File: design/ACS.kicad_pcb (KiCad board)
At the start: 4 copper layers, 60 x 45 mm, 87 parts, among them IC1 ADXL375BCCZ, IC2 I3G4250DTR, IC3 TPS56A37RPAR, IC4 74HCT126D,653, J1 SM06B-SRSS-TBLFSN, J2 XT30, J3 USB_C_Receptacle_USB2.0_14P, J4 SM04B-SRSS-TB, M1 Servo_W, M2 Servo_S, M3 Servo_E, M4 Servo_N, U1 STM32U575CGUx, U2 USBLC6-2SC6, U3 SN65HVD232, Y1 16MHz

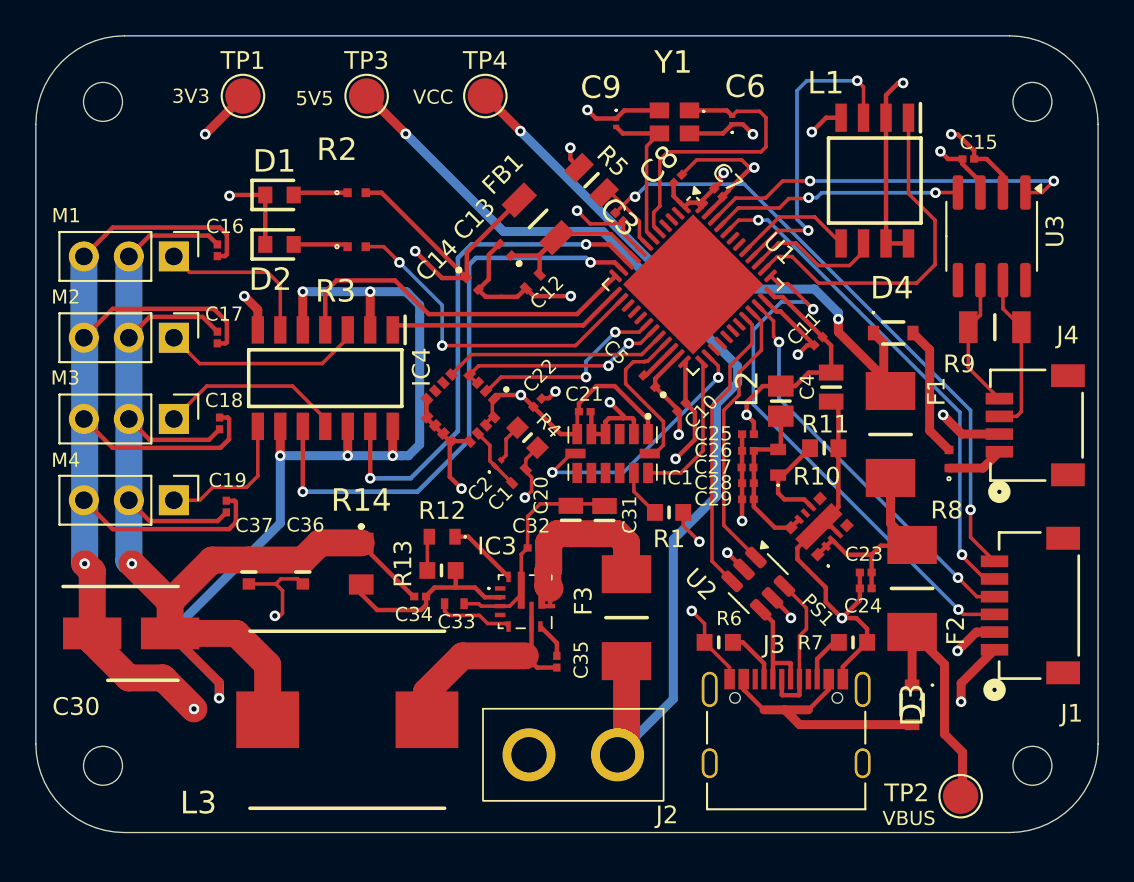
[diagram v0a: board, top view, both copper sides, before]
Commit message: fix footprint assignment and add BOM
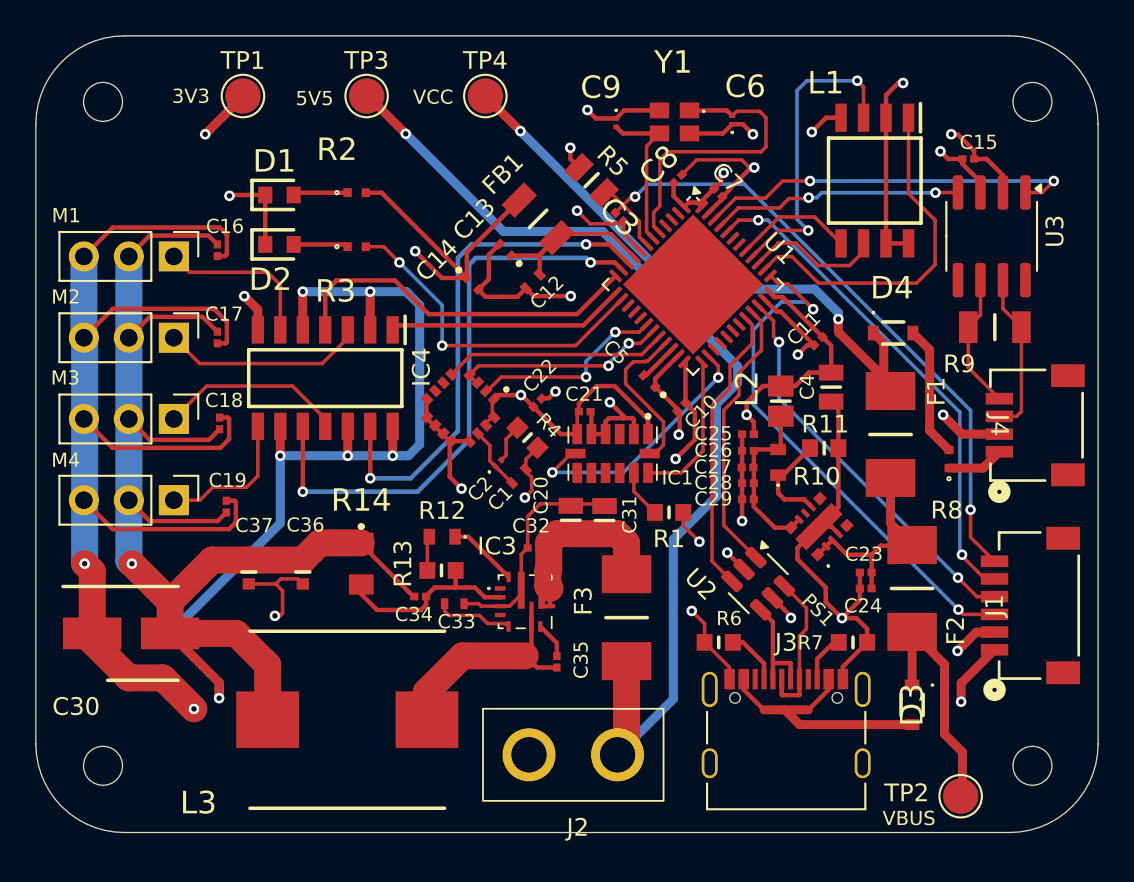
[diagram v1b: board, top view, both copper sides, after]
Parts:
- J1: footprint ACS:CONN_SM06B-SRSS-TB_JST -> footprints:CONN_SM06B-SRSS-TB_JST
- J2: footprint ACS:XT30 -> footprints:XT30
- J3: footprint Connector_USB:USB_C_Receptacle_Palconn_UTC16-G -> footprints:USB_C_Receptacle_Palconn_UTC16-G fixed
- J4: footprint ACS:CONN_SM04B-SRSS-TB_JST -> footprints:CONN_SM04B-SRSS-TB_JST
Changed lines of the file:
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@@
 		)
 	)
-	(footprint "ACS:XT30"
+	(footprint "footprints:XT30"
 		(layer "F.Cu")
 		(at 136.565 119.38)
 		(property "Reference" "J2"
-			(at 5.294 3.4036 0)
+			(at 0.254 4.112 0)
 			(unlocked yes)
 			(layer "F.SilkS")
@@
 		)
 		(property "Value" "XT30"
-			(at -3.342 3.6322 0)
+			(at 0.254 5.612 0)
 			(unlocked yes)
 			(layer "F.Fab")
@@
 		)
 		(fp_text user "${REFERENCE}"
-			(at 5.548 3.5814 0)
+			(at 0.254 7.112 0)
 			(unlocked yes)
 			(layer "F.Fab")
@@
 		(embedded_fonts no)
 	)
-	(footprint "ACS:CONN_SM04B-SRSS-TB_JST"
+	(footprint "footprints:CONN_SM04B-SRSS-TB_JST"
 		(layer "F.Cu")
 		(at 162.7281 100.7632 -90)
 		(tags "SM04B-SRSS-TB ")
 		(property "Reference" "J4"
-			(at -5.0814 -1.7623 0)
+			(at 0 2.0985 270)
 			(unlocked yes)
 			(layer "F.SilkS")
@@
 		)
 		(property "Datasheet" "SM04B-SRSS-TB"
-			(at 0 0 90)
+			(at 0 0 270)
 			(layer "F.Fab")
 			(hide yes)
@@
 		)
 		(property "Description" ""
-			(at 0 0 90)
+			(at 0 0 270)
 			(layer "F.Fab")
 			(hide yes)
@@
 		)
 	)
-	(footprint "Connector_USB:USB_C_Receptacle_Palconn_UTC16-G"
+	(footprint "footprints:USB_C_Receptacle_Palconn_UTC16-G fixed"
 		(layer "F.Cu")
 		(at 148.59 117.616)
@@
 		(tags "USB C Type-C Receptacle USB2.0")
 		(property "Reference" "J3"
-			(at -0.6858 -4.459 0)
+			(at 0 -4.58 0)
 			(layer "F.SilkS")
 			(effects
@@
 		)
 		(property "Value" "USB_C_Receptacle_USB2.0_14P"
-			(at -0.127 3.669 0)
+			(at 0 6.24 0)
 			(layer "F.Fab")
 			(effects
@@
 		(sheetname "/")
 		(sheetfile "ACS.kicad_sch")
+		(clearance 0.1)
 		(attr smd)
 		(fp_line
@@
 		)
 		(fp_text user "${REFERENCE}"
-			(at 5.8928 5.3454 0)
+			(at 0 1.18 0)
 			(layer "F.Fab")
 			(effects
@@
 			(drill 0.6)
 			(layers "F&B.Cu" "*.Mask")
+			(clearance 0)
 		)
 		(pad "" np_thru_hole circle
@@
 			(size 0.6 0.6)
 			(drill 0.6)
-			(layers "*.Cu" "*.Mask")
+			(layers "F&B.Cu" "*.Mask")
+			(clearance 0)
 		)
 		(pad "A1" smd rect
@@
 			(layers "*.Cu" "*.Mask")
 			(remove_unused_layers no)
-			(net 35 "unconnected-(J3-SHIELD-PadS1)_1")
+			(net 32 "unconnected-(J3-SHIELD-PadS1)")
 			(pinfunction "SHIELD")
 			(pintype "passive+no_connect")
@@
 			(layers "*.Cu" "*.Mask")
 			(remove_unused_layers no)
-			(net 32 "unconnected-(J3-SHIELD-PadS1)")
+			(net 35 "unconnected-(J3-SHIELD-PadS1)_1")
 			(pinfunction "SHIELD")
 			(pintype "passive+no_connect")
@@
 		)
 	)
-	(footprint "ACS:CONN_SM06B-SRSS-TB_JST"
+	(footprint "footprints:CONN_SM06B-SRSS-TB_JST"
 		(layer "F.Cu")
 		(at 162.8648 110.9472 90)
 		(tags "SM06B-SRSS-TBLFSN ")
 		(property "Reference" "J1"
-			(at -6.096 1.8542 0)
+			(at 0 -2.506701 90)
 			(unlocked yes)
 			(layer "F.SilkS")

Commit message: add gnd test
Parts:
- added TP5: TestPoint, TestPoint:TestPoint_Pad_D2.0mm, F.Cu at (112.9, 86.8)
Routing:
- net Earth: track 209.7 -> 213.4 mm, vias 25 -> 26
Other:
- board text added: "GND"
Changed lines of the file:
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@@
 		)
 	)
+	(footprint "TestPoint:TestPoint_Pad_D2.0mm"
+		(layer "F.Cu")
+		(at 112.8522 86.832)
+		(descr "SMD pad as test Point, diameter 2.0mm")
+		(tags "test point SMD pad")
+		(property "Reference" "TP5"
+			(at 0 -1.998 0)
+			(layer "F.SilkS")
+			(effects
+				(font
+					(size 1 1)
+					(thickness 0.15)
+				)
+			)
+		)
+		(property "Value" "TestPoint"
+			(at 0 2.05 0)
+			(layer "F.Fab")
+			(effects
+				(font
+					(size 1 1)
+					(thickness 0.15)
+				)
+			)
+		)
+		(property "Datasheet" "~"
+			(at 0 0 0)
+			(unlocked yes)
+			(layer "F.Fab")
+			(hide yes)
+			(effects
+				(font
+					(size 1.27 1.27)
+					(thickness 0.15)
+				)
+			)
+		)
+		(property "Description" "test point"
+			(at 0 0 0)
+			(unlocked yes)
+			(layer "F.Fab")
+			(hide yes)
+			(effects
+				(font
+					(size 1.27 1.27)
+					(thickness 0.15)
+				)
+			)
+		)
+		(property ki_fp_filters "Pin* Test*")
+		(sheetname "/")
+		(sheetfile "ACS.kicad_sch")
+		(attr exclude_from_pos_files)
+		(fp_circle
+			(center 0 0)
+			(end 0 1.2)
+			(stroke
+				(width 0.12)
+				(type solid)
+			)
+			(fill no)
+			(layer "F.SilkS")
+		)
+		(fp_circle
+			(center 0 0)
+			(end 1.5 0)
+			(stroke
+				(width 0.05)
+				(type solid)
+			)
+			(fill no)
+			(layer "F.CrtYd")
+		)
+		(fp_text user "${REFERENCE}"
+			(at 0 -2 0)
+			(layer "F.Fab")
+			(effects
+				(font
+					(size 1 1)
+					(thickness 0.15)
+				)
+			)
+		)
+		(pad "1" smd circle
+			(at 0 0)
+			(size 2 2)
+			(layers "F.Cu" "F.Mask")
+			(net 1 "Earth")
+			(pinfunction "1")
+			(pintype "passive")
+		)
+		(embedded_fonts no)
+	)
 	(footprint "SamacSys_Parts:GRM033D70J224ME01D"
 		(layer "F.Cu")
@@
 			(layers "*.Cu" "*.Mask")
 			(remove_unused_layers no)
-			(net 32 "unconnected-(J3-SHIELD-PadS1)")
+			(net 37 "unconnected-(J3-SHIELD-PadS1)_2")
 			(pinfunction "SHIELD")
 			(pintype "passive+no_connect")
@@
 			(layers "*.Cu" "*.Mask")
 			(remove_unused_layers no)
-			(net 37 "unconnected-(J3-SHIELD-PadS1)_2")
+			(net 32 "unconnected-(J3-SHIELD-PadS1)")
 			(pinfunction "SHIELD")
 			(pintype "passive+no_connect")
@@
 		)
 	)
+	(gr_text "GND"
+		(at 114.6556 86.8426 0)
+		(layer "F.SilkS")
+		(effects
+			(font
+				(size 0.8 0.8)
+				(thickness 0.1)
+			)
+			(justify left bottom)
+		)
+	)
 	(gr_text "5V5"
 		(at 120.8786 82.7786 0)
@@
 	)
 	(segment
+		(start 112.8522 86.832)
+		(end 109.2052 86.832)
+		(width 0.254)
+		(layer "F.Cu")
+		(net 1)
+	)
+	(segment
 		(start 133.8834 103.251)
 		(end 133.8834 102.6926)
@@
 	)
 	(segment
+		(start 109.2052 86.832)
+		(end 109.1946 86.8426)
+		(width 0.254)
+		(layer "F.Cu")
+		(net 1)
+	)
+	(segment
 		(start 110.553 89.597)
 		(end 108.92 91.23)
@@
 		(size 0.6)
 		(drill 0.3)
+		(layers "F.Cu" "B.Cu")
+		(net 1)
+	)
+	(via
+		(at 109.1946 86.8426)
+		(size 0.6)
+		(drill 0.3)

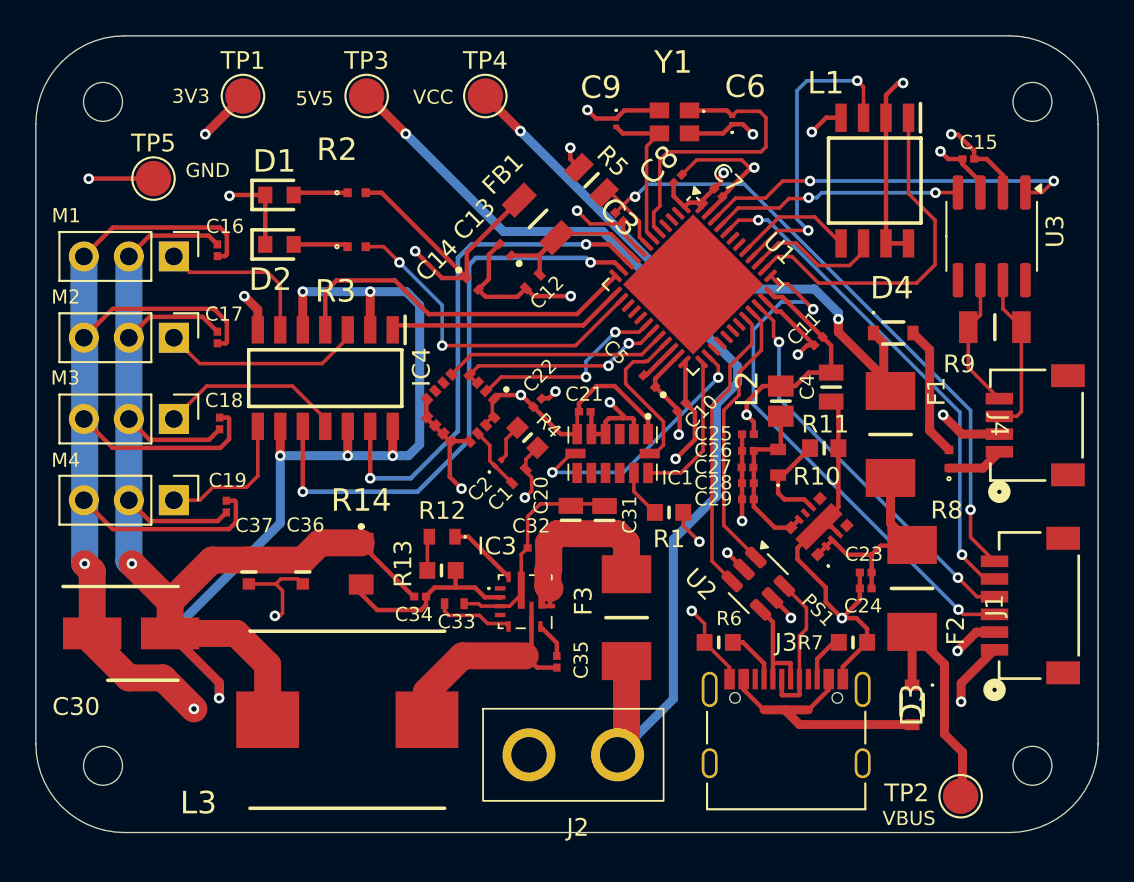
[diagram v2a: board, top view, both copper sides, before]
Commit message: move servo 5V5 and GND to F
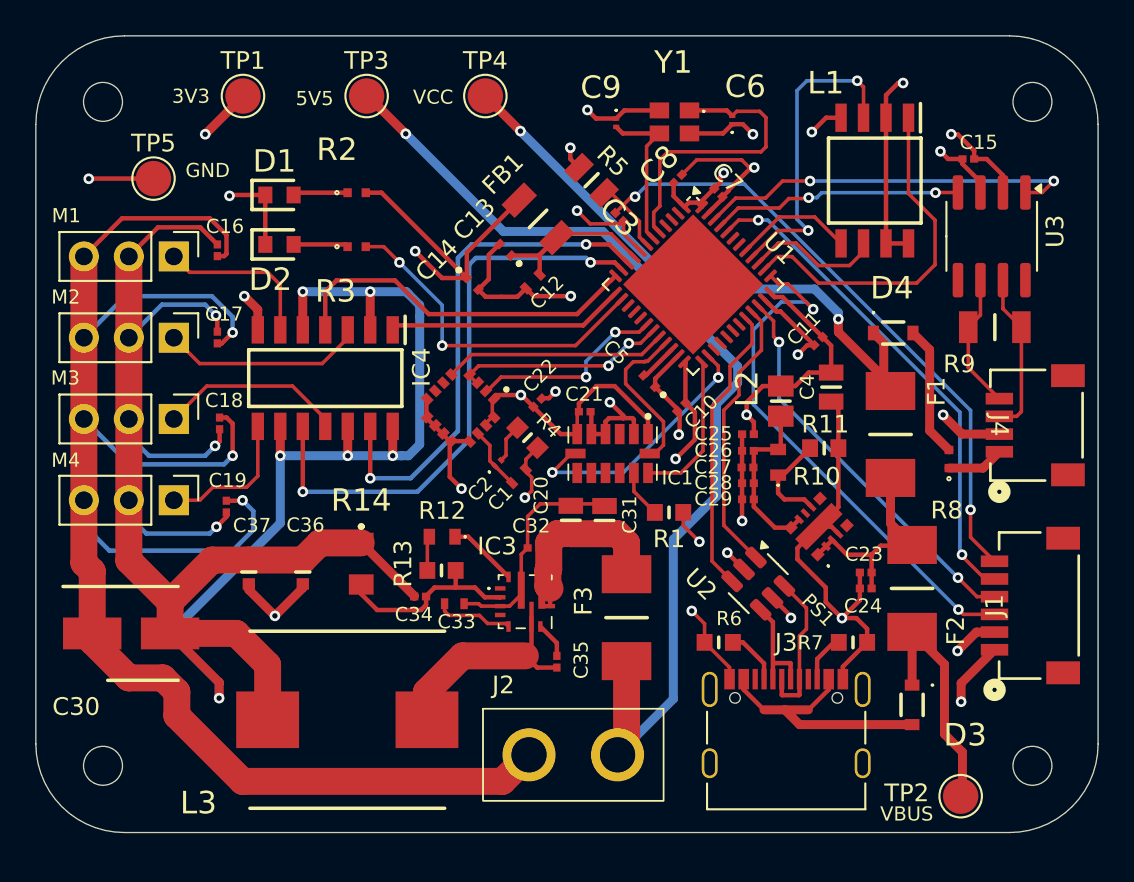
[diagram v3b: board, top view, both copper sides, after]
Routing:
- net Earth: track 213.4 -> 241.5 mm, vias 26 -> 27
- net +5V5: track 125.7 -> 130.2 mm, vias 7 -> 9

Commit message: design review fixes
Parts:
- moved C12 4.86 mm to (138.1, 89.6), turned to 135 degrees
- moved FB1 2.88 mm to (133.5, 91.8)
- moved C13 2.66 mm to (135.0, 89.6)
- moved C15 1.30 mm to (160.2, 85.9)
- moved C14 0.92 mm to (130.1, 92.2), turned to 135 degrees
- moved C10 0.26 mm to (142.8, 99.5)
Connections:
- J3 pad S1: unconnected-(J3-SHIELD-PadS1)_3 -> Earth
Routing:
- net Earth: track 241.5 -> 146.7 mm, vias 27 -> 28
- net +3V3: track 81.3 -> 68.2 mm, vias 11 -> 10
- net /SERVO_PWM_N: track 29.1 -> 26.0 mm
- net /SERVO_PWM_E: track 33.3 -> 30.2 mm
- net +3V3A: track 10.9 -> 8.52 mm
- net +5V5: track 130.2 -> 128.4 mm, vias 9 -> 6
- net /SWCLK: track 30.1 -> 28.8 mm
- net /NRST: track 39.4 -> 40.7 mm
- net /ACC_SDIO: track 8.68 -> 9.39 mm
- net Net-(IC4-3Y): track 8.12 -> 7.51 mm
- net /CAN_TX: track 21.9 -> 22.5 mm

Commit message: design review fixes
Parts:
- removed the C25 at (146.4, 101.3)
- removed the C26 at (146.4, 102.2)
- removed the C27 at (146.4, 103.1)
- removed the L2 at (148.3, 99.4)
- added C11: 22u, SamacSys_Parts:GRM18x, F.Cu at (147.6, 104.4)
- added C35: 100n, SamacSys_Parts:CAPC0603X35N, F.Cu at (126.7, 102.5)
- added C36: 100n, SamacSys_Parts:CAPC0603X35N, F.Cu at (121.0, 93.6)
- added C37: 100n, SamacSys_Parts:CAPC0603X35N, F.Cu at (124.7, 93.6)
- C28, C29: value 4u7 -> 100n; footprint SamacSys_Parts:CAPC0603X55N -> SamacSys_Parts:CAPC0603X35N
- moved C29 26.9 mm to (119.7, 102.5), turned to 180 degrees
- moved C28 23.0 mm to (123.5, 102.4), turned to 180 degrees
- moved R3 3.04 mm to (150.7, 101.2), turned to 180 degrees
- moved C17 2.60 mm to (142.9, 83.4), turned to -45 degrees
- moved U2 2.46 mm to (148.3, 111.8), turned to -90 degrees
- moved Y1 2.33 mm to (140.7, 85.4), turned to 135 degrees
- moved R11 1.75 mm to (143.0, 113.1)
- moved C5 1.67 mm to (153.2, 110.7)
- moved C4 1.60 mm to (153.2, 111.6)
- moved F2 1.35 mm to (154.4, 99.9)
- moved D4 1.33 mm to (154.8, 94.2)
- moved F3 1.13 mm to (155.8, 108.9)
- moved PS1 1.11 mm to (151.5, 106.5), turned to 180 degrees
- moved C16 0.99 mm to (151.2, 97.6)
- moved C20 0.99 mm to (143.5, 86.8)
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- renumbered C21 to C1, C22 to C10, C36 to C12, C1 to C13, C2 to C14, C37 to C15, C4 to C16, C6 to C17, C7 to C18, C3 to C19, C20 to C2, C8 to C20, C9 to C21, C5 to C22, C10 to C23, C11 to C24, C12 to C25, C13 to C26, C14 to C27, C31 to C3, C16 to C30, C17 to C31, C18 to C32, C15 to C33, C19 to C34, C30 to C38, C24 to C4, C23 to C5, C32 to C6, C33 to C7, C35 to C8, C34 to C9, F3 to F1, F1 to F2, F2 to F3, IC3 to IC2, IC2 to IC3, J2 to J1, J1 to J2, L3 to L2, R12 to R1, R5 to R10, R6 to R11, R7 to R12, R8 to R13, R9 to R14, R1 to R2, R10 to R3, R11 to R4, R14 to R5, R13 to R6, R2 to R7, R3 to R8, R4 to R9, TP3 to TP1, TP4 to TP2, TP2 to TP3, TP5 to TP4, TP1 to TP5
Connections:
- C1 pad 1: +3V3 -> +3V3A
- C10 pad 1: +3V3 -> +3V3A
- C28 pad 1: Earth -> +5V5
- C28 pad 2: Net-(PS1-VOUT_1) -> Earth
- C29 pad 1: Earth -> +5V5
- C29 pad 2: Net-(PS1-VOUT_1) -> Earth
- IC1 pad 1: +3V3 -> +3V3A
- IC1 pad 6: +3V3 -> +3V3A
- IC3 pad 1: +3V3 -> +3V3A
- IC3 pad 15: +3V3 -> +3V3A
- IC3 pad 16: +3V3 -> +3V3A
- PS1 pad 10: Net-(PS1-VOUT_1) -> +3V3
- PS1 pad 9: Net-(PS1-VOUT_1) -> +3V3
- R3 pad 2: Net-(PS1-VOUT_1) -> +3V3
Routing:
- net Earth: track 146.7 -> 176.5 mm, vias 28 -> 30
- net +3V3A: track 8.52 -> 32.0 mm, vias 0 -> 2
- net Net-(PS1-VOUT_1): track 9.79 -> 0.00 mm
- net /OSC_IN: track 17.0 -> 7.54 mm
- net /NRST: track 40.7 -> 48.8 mm
- net Net-(PS1-EN): track 12.4 -> 20.5 mm
- net +5V5: track 128.4 -> 136.2 mm
- net +3V3: track 68.2 -> 74.4 mm, vias 10 -> 9
- net /USB_D_P: track 15.7 -> 21.8 mm
- net /USB_D_N: track 16.4 -> 21.3 mm
- net /SERVO_PWM_N: track 26.0 -> 30.6 mm
- net /SERVO_PWM_E: track 30.2 -> 34.4 mm
- net /USB_ESD_P: track 8.73 -> 4.68 mm
- net /BOOT0: track 28.7 -> 31.2 mm
- net VBUS: track 13.5 -> 15.8 mm
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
